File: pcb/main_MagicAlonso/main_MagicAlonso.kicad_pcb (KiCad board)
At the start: 2 copper layers, 140 x 200 mm, 0 parts

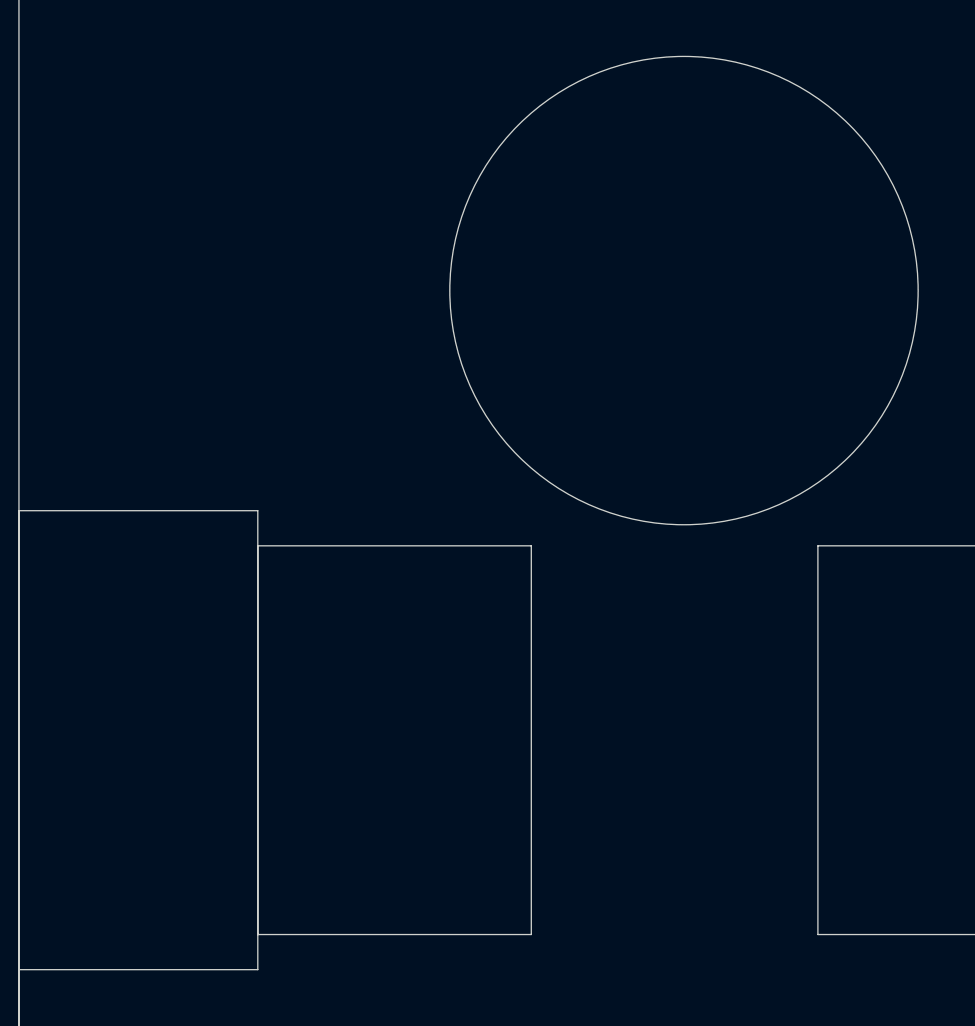
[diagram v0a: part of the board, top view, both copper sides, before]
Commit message: Schematic & PCB updates
made advancements on the schematic circuits and the PCB layout drawings.
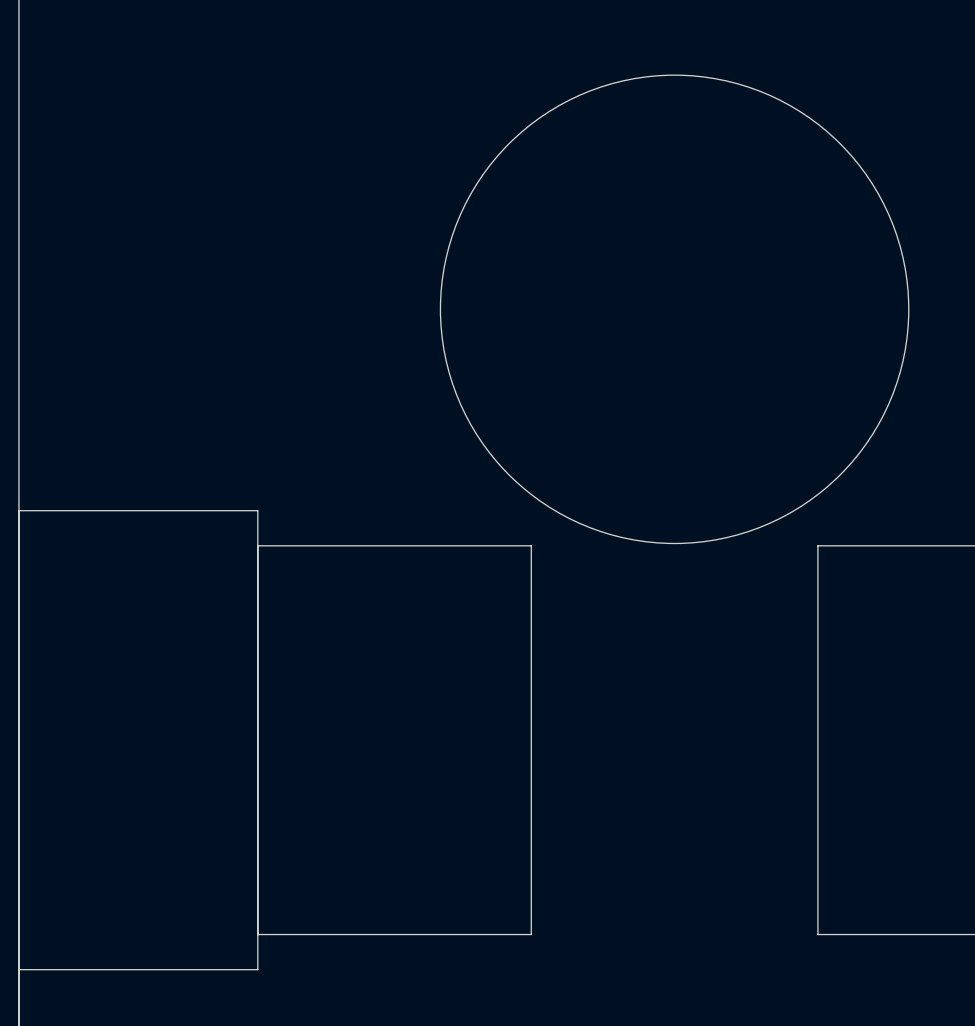
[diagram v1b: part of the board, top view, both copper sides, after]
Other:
- outline, holes or cut-outs redrawn
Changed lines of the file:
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@@
 	(net 0 "")
+	(gr_line
+		(start 106.5 238.5)
+		(end 106.5 38.5)
+		(stroke
+			(width 0.05)
+			(type dash)
+		)
+		(layer "Dwgs.User")
+	)
+	(gr_line
+		(start 121.8 183.25)
+		(end 91.2 183.25)
+		(stroke
+			(width 0.05)
+			(type dash)
+		)
+		(layer "Dwgs.User")
+	)
 	(gr_line
 		(start 176.5 238.5)
@@
 	)
 	(gr_rect
-		(start 62 224.75)
-		(end 91.2 183.25)
-		(stroke
-			(width 0.05)
-			(type solid)
-		)
-		(fill no)
-		(layer "Edge.Cuts")
-	)
-	(gr_rect
-		(start 151 224.75)
-		(end 121.8 183.25)
+		(start 62 183.25)
+		(end 91.2 224.75)
+		(stroke
+			(width 0.05)
+			(type solid)
+		)
+		(fill no)
+		(layer "Edge.Cuts")
+	)
+	(gr_rect
+		(start 121.8 183.25)
+		(end 151 224.75)
 		(stroke
 			(width 0.05)
@@
 	)
 	(gr_circle
-		(center 107.5 156)
-		(end 132.5 156)
+		(center 106.5 158)
+		(end 131.5 158)
 		(stroke
 			(width 0.05)
@@
 	)
 	(gr_rect
-		(start 36.5 228.5)
-		(end 62 179.5)
+		(start 36.5 179.5)
+		(end 62 228.5)
 		(stroke
 			(width 0.05)
@@
 	)
 	(gr_rect
-		(start 176.5 228.5)
-		(end 151 179.5)
+		(start 151 179.5)
+		(end 176.5 228.5)
 		(stroke
 			(width 0.05)
@@
 		(layer "Edge.Cuts")
 	)
+	(dimension
+		(type orthogonal)
+		(layer "Dwgs.User")
+		(pts
+			(xy 121.8 225.25) (xy 91.2 225.25)
+		)
+		(height 18.25)
+		(orientation 0)
+		(format
+			(prefix "")
+			(suffix "")
+			(units 3)
+			(units_format 0)
+			(precision 4)
+			(suppress_zeroes yes)
+		)
+		(style
+			(thickness 0.05)
+			(arrow_length 1.27)
+			(text_position_mode 0)
+			(arrow_direction outward)
+			(extension_height 0.58642)
+			(extension_offset 0.5)
+			(keep_text_aligned yes)
+		)
+		(gr_text "30,6"
+			(at 106.5 241.35 0)
+			(layer "Dwgs.User")
+			(effects
+				(font
+					(size 2 2)
+					(thickness 0.15)
+				)
+			)
+		)
+	)
+	(dimension
+		(type orthogonal)
+		(layer "Dwgs.User")
+		(pts
+			(xy 176.5 241) (xy 36.5 241)
+		)
+		(height 8)
+		(orientation 0)
+		(format
+			(prefix "")
+			(suffix "")
+			(units 3)
+			(units_format 0)
+			(precision 4)
+			(suppress_zeroes yes)
+		)
+		(style
+			(thickness 0.05)
+			(arrow_length 1.27)
+			(text_position_mode 0)
+			(arrow_direction outward)
+			(extension_height 0.58642)
+			(extension_offset 0.5)
+			(keep_text_aligned yes)
+		)
+		(gr_text "140"
+			(at 106.5 246.85 0)
+			(layer "Dwgs.User")
+			(effects
+				(font
+					(size 2 2)
+					(thickness 0.15)
+				)
+			)
+		)
+	)
+	(dimension
+		(type orthogonal)
+		(layer "Dwgs.User")
+		(pts
+			(xy 36.5 228.5) (xy 36.5 238.5)
+		)
+		(height -4.5)
+		(orientation 1)
+		(format
+			(prefix "")
+			(suffix "")
+			(units 3)
+			(units_format 0)
+			(precision 4)
+			(suppress_zeroes yes)
+		)
+		(style
+			(thickness 0.05)
+			(arrow_length 1.27)
+			(text_position_mode 0)
+			(arrow_direction outward)
+			(extension_height 0.58642)
+			(extension_offset 0.5)
+			(keep_text_aligned yes)
+		)
+		(gr_text "10"
+			(at 29.85 233.5 90)
+			(layer "Dwgs.User")
+			(effects
+				(font
+					(size 2 2)
+					(thickness 0.15)
+				)
+			)
+		)
+	)
+	(dimension
+		(type orthogonal)
+		(layer "Dwgs.User")
+		(pts
+			(xy 176.5 228.5) (xy 176.5 238.5)
+		)
+		(height 6.5)
+		(orientation 1)
+		(format
+			(prefix "")
+			(suffix "")
+			(units 3)
+			(units_format 0)
+			(precision 4)
+			(suppress_zeroes yes)
+		)
+		(style
+			(thickness 0.05)
+			(arrow_length 1.27)
+			(text_position_mode 0)
+			(arrow_direction outward)
+			(extension_height 0.58642)
+			(extension_offset 0.5)
+			(keep_text_aligned yes)
+		)
+		(gr_text "10"
+			(at 180.85 233.5 90)
+			(layer "Dwgs.User")
+			(effects
+				(font
+					(size 2 2)
+					(thickness 0.15)
+				)
+			)
+		)
+	)
 	(group ""

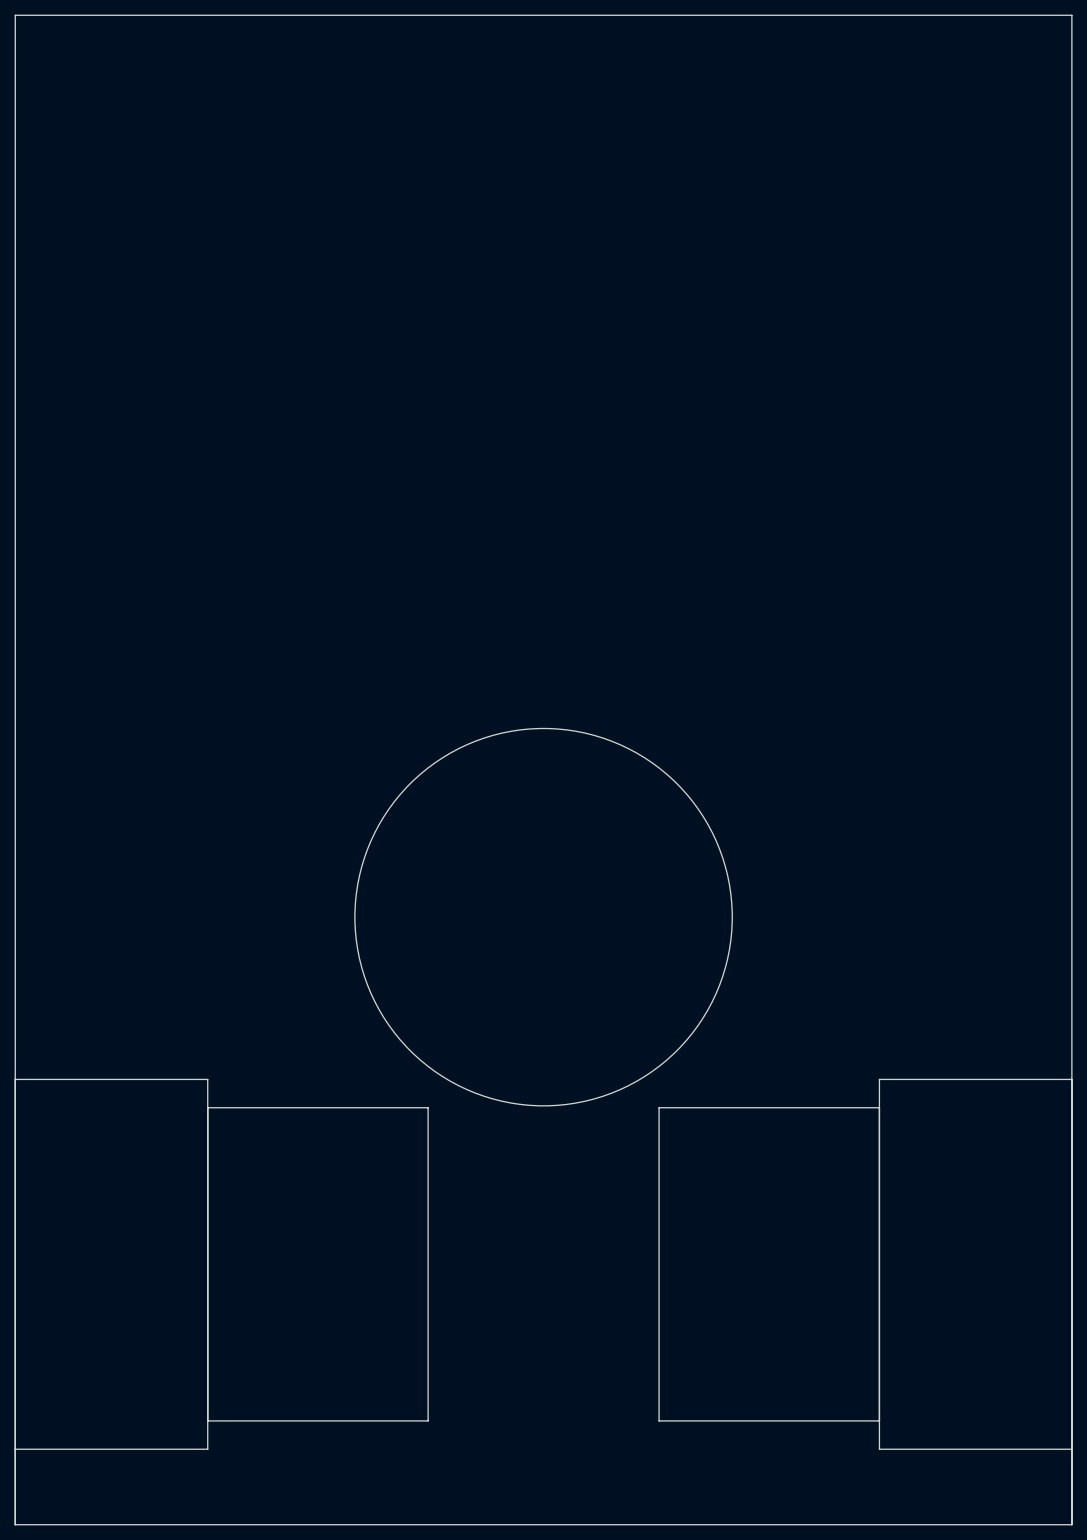
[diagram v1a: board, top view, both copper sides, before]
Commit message: Big changes PCB
Advancements on the schematic were made:
- Completed MP2315 circuit
- Passive Buzzer
- Mounting holes & other symbols added

Also the PCB drawings were improved.
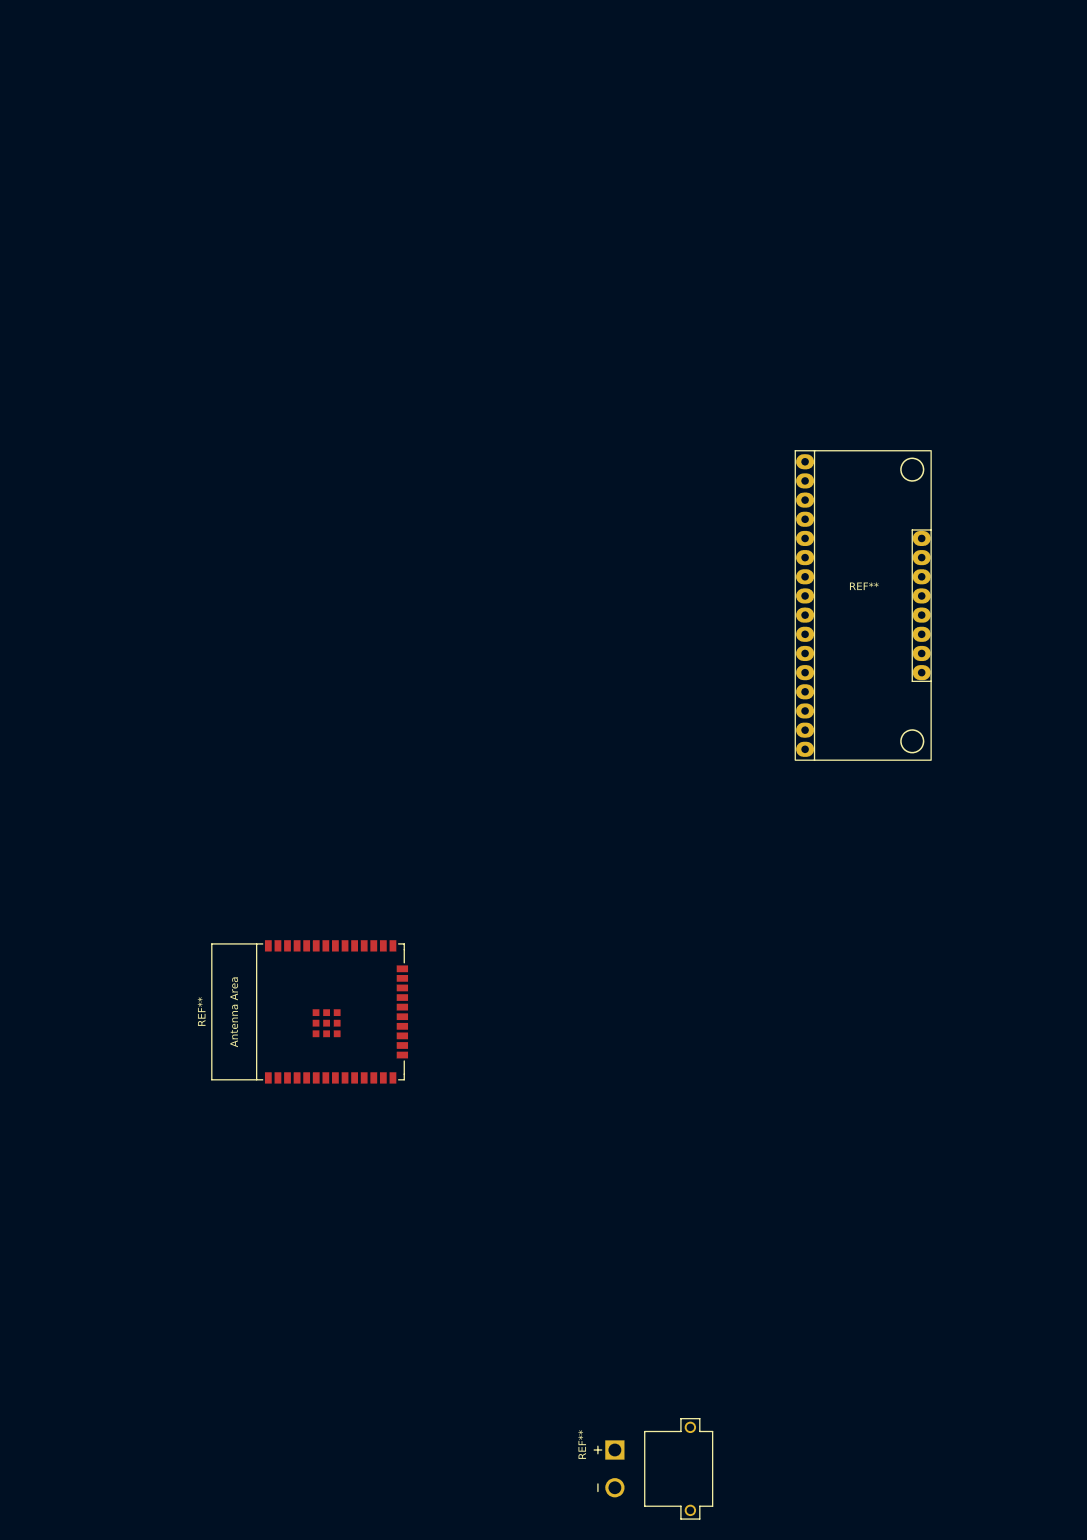
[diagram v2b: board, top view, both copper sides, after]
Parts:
- added REF**: HP4067_module, MixLib:HP4067_module, F.Cu at (148.9, 116.5)
- added REF**: ESP32-WROOM-32E, PCM_Espressif:ESP32-WROOM-32E, F.Cu at (77.0, 170.6)
- added REF**: AMASS_XT30PW-M, MixLib:XT30PW-M, F.Cu at (126.0, 231.1)
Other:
- board outline removed
- board text added: "+"
- board text added: "-"
- board text added: "1"
- board text added: "2"
- board text added: "3"
- board text added: "ESC"

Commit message: Schematic and PCB
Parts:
- removed the REF** at (148.9, 116.5)
- moved REF** 5.58 mm to (76.5, 165.0), turned to 0 degrees

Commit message: schematic and pcb drawings
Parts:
- added BORNERA2: J**, MixLib:Bornera_2_duo, F.Cu at (102.2, 230.0)
- added BORNERA2: J**, MixLib:Bornera_2_duo, F.Cu at (91.8, 230.0)
- added BORNERA2: J**, MixLib:Bornera_2_duo, F.Cu at (112.6, 230.0)
- added REF**: TerminalBlock_MetzConnect_Type086_RT03403HBLC_1x03_P3.81mm_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, TerminalBlock_MetzConnect:TerminalBlock_MetzConnect_Type086_RT03403HBLC_1x03_P3.81mm_Horizontal, F.Cu at (128.6, 271.2)
- added REF**: Mini360, MixLib:Mini360_step-down, F.Cu at (143.2, 164.8)
- added REF**: TerminalBlock_MetzConnect_Type086_RT03403HBLC_1x03_P3.81mm_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, TerminalBlock_MetzConnect:TerminalBlock_MetzConnect_Type086_RT03403HBLC_1x03_P3.81mm_Horizontal, F.Cu at (140.4, 271.2)
- added REF**: SOIC-8-1EP_3.9x4.9mm_P1.27mm_EP2.29x3mm, Package_SO:SOIC-8-1EP_3.9x4.9mm_P1.27mm_EP2.29x3mm, B.Cu at (116.8, 217.7)
- added REF**: SOIC-8-1EP_3.9x4.9mm_P1.27mm_EP2.29x3mm, Package_SO:SOIC-8-1EP_3.9x4.9mm_P1.27mm_EP2.29x3mm, B.Cu at (101.2, 218.0)
- added REF**: SOIC-8-1EP_3.9x4.9mm_P1.27mm_EP2.29x3mm, Package_SO:SOIC-8-1EP_3.9x4.9mm_P1.27mm_EP2.29x3mm, B.Cu at (109.0, 218.2)
- moved REF** 4.67 mm to (73.0, 161.9)
- moved REF** 4.05 mm to (130.0, 231.2)
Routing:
- net (no net): track 0.00 -> 42.2 mm

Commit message: schematic updates
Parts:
- removed BORNERA2 (x3): J**, MixLib:Bornera_2_duo
- removed the REF** at (73.0, 161.9)
- removed the REF** at (140.4, 271.2)
- removed the REF** at (116.8, 217.7)
- removed the REF** at (101.2, 218.0)
- removed the REF** at (109.0, 218.2)
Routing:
- net (no net): track 42.2 -> 0.00 mm
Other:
- board text added: "1303.5 BLDC"
- board text added: "1404 BLDC"
